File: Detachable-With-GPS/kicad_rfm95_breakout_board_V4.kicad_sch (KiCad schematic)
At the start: 55 parts, among them J1 USB_B_Micro, J2 Conn_Coaxial, J3 Male Pinheader 1x20, J4 Male Pinheader 1x20, J5 Male Pinheader 1x2, J6 ARM 10pin, SW1 SW_Push, SW2 SW_Push, SW3 SW_Push, SW4 SW_Push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

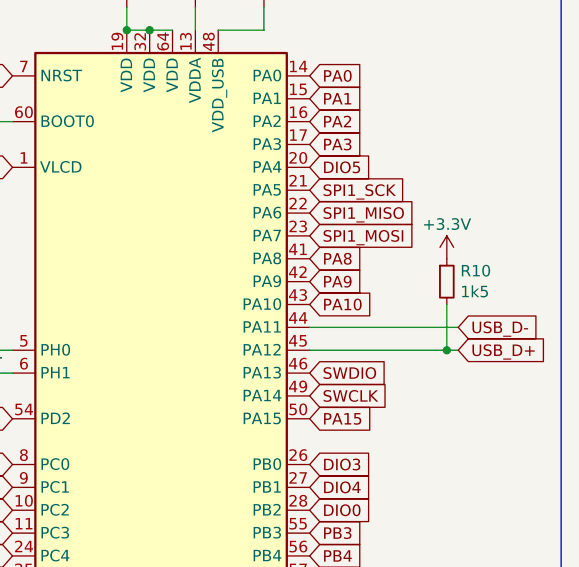
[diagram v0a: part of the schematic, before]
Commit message: Update USB Pullup (R already internal in STM32L0 processors)
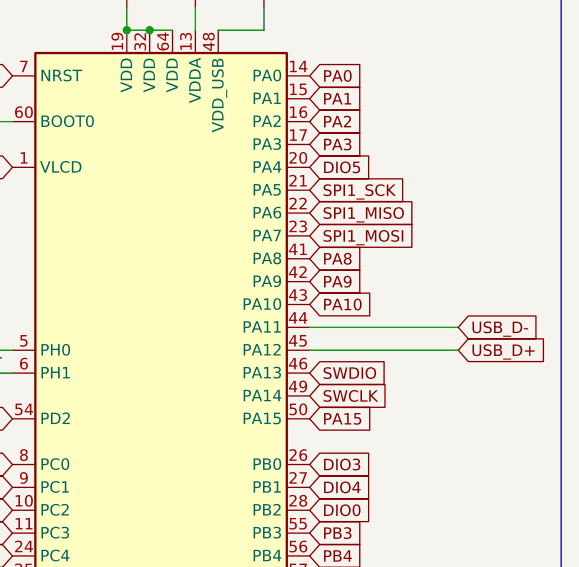
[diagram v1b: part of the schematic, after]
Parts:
- removed R10: 1k5, Resistor_SMD:R_0603_1608Metric, symbol Device:R_Small
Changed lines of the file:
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@@
   (junction (at 27.94 71.12) (diameter 0) (color 0 0 0 0)
   )
-  (junction (at 270.51 80.01) (diameter 0) (color 0 0 0 0)
-  )
   (junction (at 142.24 113.03) (diameter 0) (color 0 0 0 0)
   )
@@
     (stroke (width 0) (type default) (color 0 0 0 0))
   )
-  (wire (pts (xy 271.78 80.01) (xy 270.51 80.01))
+  (wire (pts (xy 255.27 80.01) (xy 271.78 80.01))
     (stroke (width 0) (type default) (color 0 0 0 0))
   )
@@
     (stroke (width 0) (type default) (color 0 0 0 0))
   )
-  (wire (pts (xy 270.51 74.93) (xy 270.51 80.01))
-    (stroke (width 0) (type default) (color 0 0 0 0))
-  )
   (wire (pts (xy 234.95 135.89) (xy 234.95 139.7))
     (stroke (width 0) (type default) (color 0 0 0 0))
@@
     (stroke (width 0) (type default) (color 0 0 0 0))
   )
-  (wire (pts (xy 255.27 80.01) (xy 270.51 80.01))
-    (stroke (width 0) (type default) (color 0 0 0 0))
-  )
   (wire (pts (xy 39.37 97.79) (xy 39.37 96.52))
     (stroke (width 0) (type default) (color 0 0 0 0))
@@
     (pin "1")
   )
-  (symbol (lib_id "power:+3.3V") (at 270.51 69.85 0) (unit 1)
-    (in_bom yes) (on_board yes)
-    (property "Reference" "#PWR0112" (id 0) (at 270.51 73.66 0)
-      (effects (font (size 1.27 1.27)) hide)
-    )
-    (property "Value" "+3.3V" (id 1) (at 270.51 66.04 0))
-    (property "Footprint" "" (id 2) (at 270.51 69.85 0)
-      (effects (font (size 1.27 1.27)) hide)
-    )
-    (property "Datasheet" "" (id 3) (at 270.51 69.85 0)
-      (effects (font (size 1.27 1.27)) hide)
-    )
-    (pin "1")
-  )
   (symbol (lib_id "Jumper:SolderJumper_2_Open") (at 142.24 36.83 0) (unit 1)
     (in_bom yes) (on_board yes)
@@
     (pin "2")
   )
-  (symbol (lib_id "Device:R_Small") (at 270.51 72.39 0) (unit 1)
-    (in_bom yes) (on_board yes)
-    (property "Reference" "R10" (id 0) (at 272.0086 71.2216 0)
-      (effects (font (size 1.27 1.27)) (justify left))
-    )
-    (property "Value" "1k5" (id 1) (at 272.0086 73.533 0)
-      (effects (font (size 1.27 1.27)) (justify left))
-    )
-    (property "Footprint" "Resistor_SMD:R_0603_1608Metric" (id 2) (at 270.51 72.39 0)
-      (effects (font (size 1.27 1.27)) hide)
-    )
-    (property "Datasheet" "~" (id 3) (at 270.51 72.39 0)
-      (effects (font (size 1.27 1.27)) hide)
-    )
-    (property "LCSC Part #" "C22842" (id 4) (at 270.51 72.39 0)
-      (effects (font (size 1.27 1.27)) hide)
-    )
-    (pin "1")
-    (pin "2")
-  )
   (symbol (lib_id "Device:C_Small") (at 127 172.72 0) (unit 1)
     (in_bom yes) (on_board yes)
@@
       (reference "#PWR0111") (unit 1) (value "GND") (footprint "")
     )
-    (path "/4f3888df-be3d-449f-8adb-f632853178bd"
-      (reference "#PWR0112") (unit 1) (value "+3.3V") (footprint "")
-    )
     (path "/a8ceb4bd-7ecb-46bf-b88f-f6b766e68534"
       (reference "#PWR0113") (unit 1) (value "+3.3V") (footprint "")
@@
       (reference "R9") (unit 1) (value "10k") (footprint "Resistor_SMD:R_0603_1608Metric")
     )
-    (path "/e28b95d5-8000-4f1f-8b75-c99b1a0583f5"
-      (reference "R10") (unit 1) (value "1k5") (footprint "Resistor_SMD:R_0603_1608Metric")
-    )
     (path "/9d4ba538-f0d9-4a7b-a404-ebdd6a64da42"
